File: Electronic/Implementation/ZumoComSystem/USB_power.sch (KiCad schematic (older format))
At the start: 9 parts, among them J2 USB_B_Micro, U6 R1218N021A

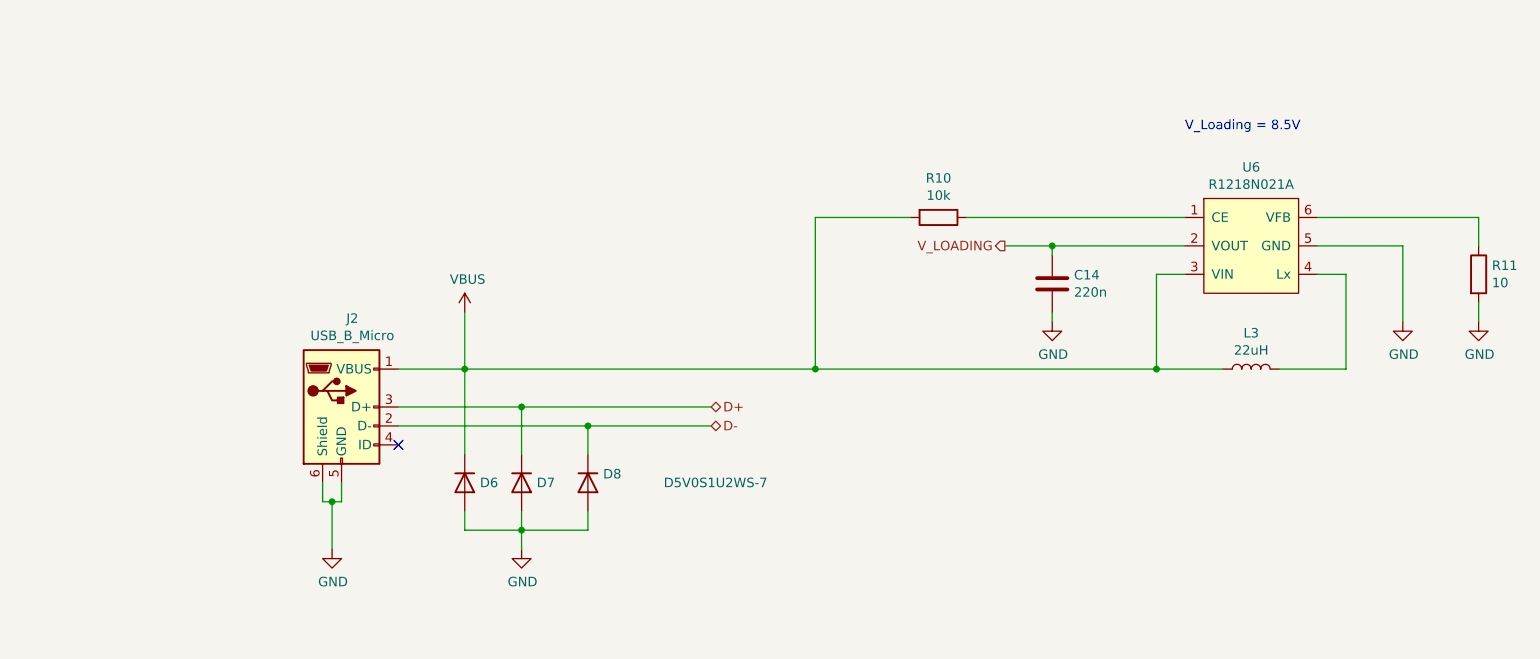
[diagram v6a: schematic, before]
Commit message: Electronic: implementation of the connector for external charging (reverse polarity protected)
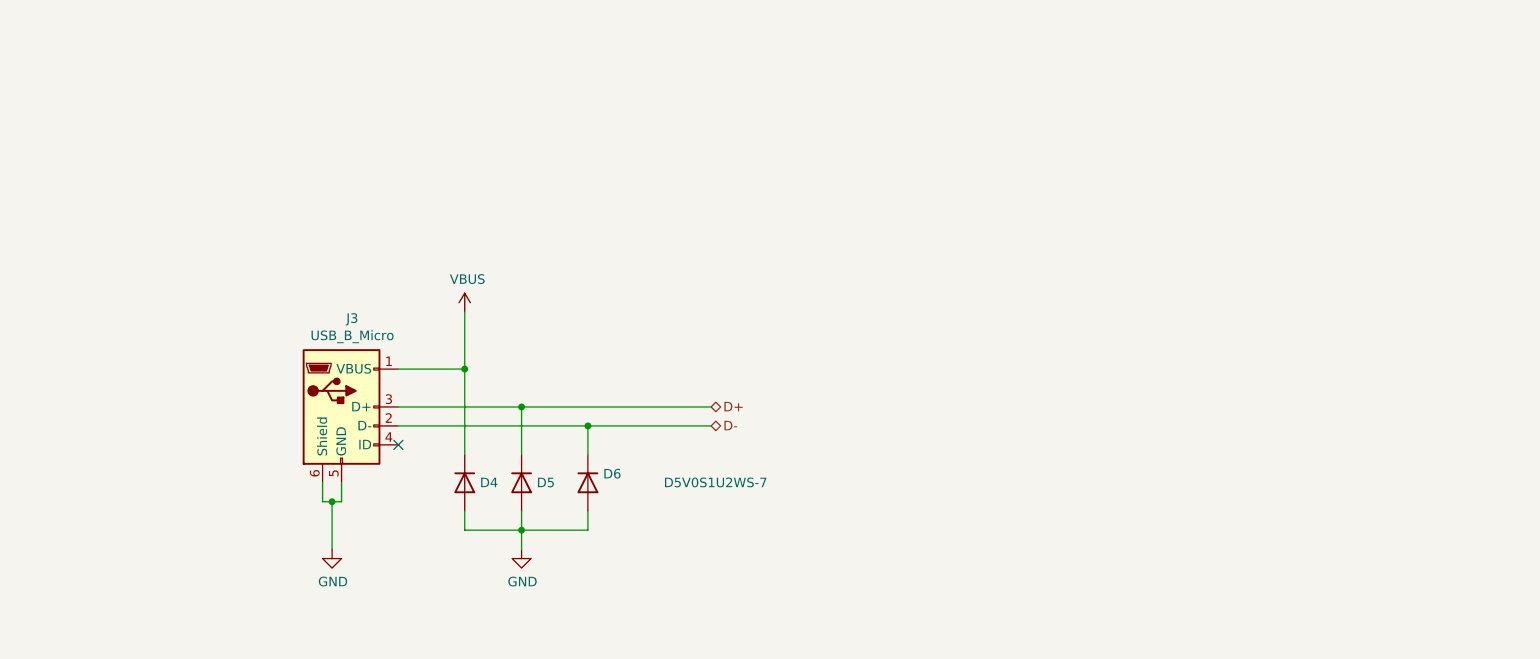
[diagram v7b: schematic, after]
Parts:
- removed C14: 220n, Capacitor_SMD:C_0603_1608Metric_Pad1.05x0.95mm_HandSolder, symbol Device:C
- removed L3: 22uH, footprints:L_Wuerth_HCI-1350_3D, symbol Device:L
- removed R10: 10k, Resistor_SMD:R_0603_1608Metric_Pad1.05x0.95mm_HandSolder, symbol Device:R
- removed R11: 10, Resistor_SMD:R_0603_1608Metric_Pad1.05x0.95mm_HandSolder, symbol Device:R
- removed U6: R1218N021A, Package_TO_SOT_SMD:SOT-23-6_Handsoldering, symbol LT1374CS8-5PBF:R1218N021A
- renumbered D6 to D4, D7 to D5, D8 to D6, J2 to J3
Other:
- note removed: "V_Loading = 8.5V"
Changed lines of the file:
@@
 Sheet 5 7
 Title "Zumo Communication System"
-Date "2022-03-08"
+Date "2022-03-25"
 Rev "V1.0"
 Comp "NewTec GmbH"
@@
 Comment4 ""
 $EndDescr
-Text HLabel 6000 2350 0    50   Output ~ 0
-V_LOADING
 Text HLabel 4450 3300 2    50   BiDi ~ 0
 D-
@@
 	2800 3200 3450 3200
 $Comp
-L Connector:USB_B_Micro J2
+L Connector:USB_B_Micro J3
 U 1 1 60DEC307
 P 2500 3200
-F 0 "J2" H 2557 3667 50  0000 C CNN
+F 0 "J3" H 2557 3667 50  0000 C CNN
 F 1 "USB_B_Micro" H 2557 3576 50  0000 C CNN
 F 2 "footprints:USB_Micro-B_Molex-105133-0001-3D" H 2650 3150 50  0001 C CNN
@@
 	2450 3700 2450 3950
 $Comp
-L power:GND #PWR030
+L power:GND #PWR026
 U 1 1 60DEDA4E
 P 2450 3950
-F 0 "#PWR030" H 2450 3700 50  0001 C CNN
+F 0 "#PWR026" H 2450 3700 50  0001 C CNN
 F 1 "GND" H 2455 3777 50  0000 C CNN
 F 2 "" H 2450 3950 50  0001 C CNN
@@
 NoConn ~ 2800 3400
 $Comp
-L LT1374CS8-5PBF:R1218N021A U6
-U 1 1 621F5235
-P 7300 2350
-F 0 "U6" H 7300 2765 50  0000 C CNN
-F 1 "R1218N021A" H 7300 2674 50  0000 C CNN
-F 2 "Package_TO_SOT_SMD:SOT-23-6_Handsoldering" H 7700 2700 50  0001 C CNN
-F 3 "https://www.nisshinbo-microdevices.co.jp/en/pdf/datasheet/r1218-ea.pdf" H 7700 2700 50  0001 C CNN
-	1    7300 2350
-	1    0    0    -1
-$EndComp
-Wire Wire Line
-	7650 2350 8100 2350
-Wire Wire Line
-	8100 2350 8100 2750
-$Comp
-L power:GND #PWR034
-U 1 1 621F66D3
-P 8100 2750
-F 0 "#PWR034" H 8100 2500 50  0001 C CNN
-F 1 "GND" H 8105 2577 50  0000 C CNN
-F 2 "" H 8100 2750 50  0001 C CNN
-F 3 "" H 8100 2750 50  0001 C CNN
-	1    8100 2750
-	1    0    0    -1
-$EndComp
-Wire Wire Line
-	6950 2350 6250 2350
-Wire Wire Line
-	6950 2200 5800 2200
-Wire Wire Line
-	5000 3000 6800 3000
-$Comp
-L Device:R R10
-U 1 1 621FAFF2
-P 5650 2200
-F 0 "R10" V 5443 2200 50  0000 C CNN
-F 1 "10k" V 5534 2200 50  0000 C CNN
-F 2 "Resistor_SMD:R_0603_1608Metric_Pad1.05x0.95mm_HandSolder" V 5580 2200 50  0001 C CNN
-F 3 "~" H 5650 2200 50  0001 C CNN
-	1    5650 2200
-	0    1    1    0
-$EndComp
-Wire Wire Line
-	5500 2200 5000 2200
-$Comp
-L Device:R R11
-U 1 1 621FB991
-P 8500 2500
-F 0 "R11" H 8570 2546 50  0000 L CNN
-F 1 "10" H 8570 2455 50  0000 L CNN
-F 2 "Resistor_SMD:R_0603_1608Metric_Pad1.05x0.95mm_HandSolder" V 8430 2500 50  0001 C CNN
-F 3 "~" H 8500 2500 50  0001 C CNN
-	1    8500 2500
-	1    0    0    -1
-$EndComp
-Wire Wire Line
-	7650 2200 8500 2200
-Wire Wire Line
-	6800 2500 6800 3000
-Wire Wire Line
-	6800 3000 7150 3000
-Wire Wire Line
-	6800 2500 6950 2500
-Wire Wire Line
-	7450 3000 7800 3000
-Wire Wire Line
-	7800 3000 7800 2500
-Wire Wire Line
-	7800 2500 7650 2500
-Wire Wire Line
-	8500 2650 8500 2750
-$Comp
-L power:GND #PWR035
-U 1 1 621FE4AA
-P 8500 2750
-F 0 "#PWR035" H 8500 2500 50  0001 C CNN
-F 1 "GND" H 8505 2577 50  0000 C CNN
-F 2 "" H 8500 2750 50  0001 C CNN
-F 3 "" H 8500 2750 50  0001 C CNN
-	1    8500 2750
-	1    0    0    -1
-$EndComp
-Wire Wire Line
-	8500 2200 8500 2350
-Connection ~ 5000 3000
-Connection ~ 6800 3000
-Wire Wire Line
-	5000 2200 5000 3000
-$Comp
-L Device:C C14
-U 1 1 62201332
-P 6250 2550
-F 0 "C14" H 6365 2596 50  0000 L CNN
-F 1 "220n" H 6365 2505 50  0000 L CNN
-F 2 "Capacitor_SMD:C_0603_1608Metric_Pad1.05x0.95mm_HandSolder" H 6288 2400 50  0001 C CNN
-F 3 "~" H 6250 2550 50  0001 C CNN
-	1    6250 2550
-	1    0    0    -1
-$EndComp
-Wire Wire Line
-	6250 2700 6250 2750
-Wire Wire Line
-	6250 2400 6250 2350
-Connection ~ 6250 2350
-Wire Wire Line
-	6250 2350 6000 2350
-$Comp
-L power:GND #PWR033
-U 1 1 62201F1D
-P 6250 2750
-F 0 "#PWR033" H 6250 2500 50  0001 C CNN
-F 1 "GND" H 6255 2577 50  0000 C CNN
-F 2 "" H 6250 2750 50  0001 C CNN
-F 3 "" H 6250 2750 50  0001 C CNN
-	1    6250 2750
-	1    0    0    -1
-$EndComp
-Text Notes 6950 1750 0    50   ~ 0
-V_Loading = 8.5V
-$Comp
-L power:VBUS #PWR031
+L power:VBUS #PWR027
 U 1 1 6230EF27
 P 3150 2700
-F 0 "#PWR031" H 3150 2550 50  0001 C CNN
+F 0 "#PWR027" H 3150 2550 50  0001 C CNN
 F 1 "VBUS" H 3165 2873 50  0000 C CNN
 F 2 "" H 3150 2700 50  0001 C CNN
@@
 	2800 3000 3150 3000
 Connection ~ 3150 3000
-Wire Wire Line
-	3150 3000 5000 3000
 $Comp
-L Device:D D7
+L Device:D D5
 U 1 1 6235853C
 P 3450 3600
-F 0 "D7" V 3450 3680 50  0000 L CNN
+F 0 "D5" V 3450 3680 50  0000 L CNN
 F 1 "D5V0S1U2WS-7" V 3495 3680 50  0001 L CNN
 F 2 "Diode_SMD:D_SOD-323_HandSoldering" H 3450 3600 50  0001 C CNN
@@
 $EndComp
 $Comp
-L Device:D D8
+L Device:D D6
 U 1 1 62358EEE
 P 3800 3600
-F 0 "D8" V 3754 3680 50  0000 L CNN
+F 0 "D6" V 3754 3680 50  0000 L CNN
 F 1 "D5V0S1U2WS-7" V 3800 4000 50  0000 L CNN
 F 2 "Diode_SMD:D_SOD-323_HandSoldering" H 3800 3600 50  0001 C CNN
@@
 	3800 3300 4450 3300
 $Comp
-L Device:D D6
+L Device:D D4
 U 1 1 62359ADA
 P 3150 3600
-F 0 "D6" V 3150 3680 50  0000 L CNN
+F 0 "D4" V 3150 3680 50  0000 L CNN
 F 1 "D5V0S1U2WS-7" V 3195 3680 50  0001 L CNN
 F 2 "Diode_SMD:D_SOD-323_HandSoldering" H 3150 3600 50  0001 C CNN
@@
 	3150 3450 3150 3000
 $Comp
-L power:GND #PWR032
+L power:GND #PWR028
 U 1 1 6235AC4B
 P 3450 3950
-F 0 "#PWR032" H 3450 3700 50  0001 C CNN
+F 0 "#PWR028" H 3450 3700 50  0001 C CNN
 F 1 "GND" H 3455 3777 50  0000 C CNN
 F 2 "" H 3450 3950 50  0001 C CNN
@@
 Wire Wire Line
 	3450 3850 3450 3950
-$Comp
-L Device:L L?
-U 1 1 623D0E3C
-P 7300 3000
-AR Path="/60C4F1BF/623D0E3C" Ref="L?"  Part="1"
-AR Path="/60C3F428/623D0E3C" Ref="L3"  Part="1"
-F 0 "L3" V 7490 3000 50  0000 C CNN
-F 1 "22uH" V 7399 3000 50  0000 C CNN
-F 2 "footprints:L_Wuerth_HCI-1350_3D" H 7300 3000 50  0001 C CNN
-F 3 "https://www.vishay.com/docs/34282/ihlp-6767gz-11.pdf" H 7300 3000 50  0001 C CNN
-	1    7300 3000
-	0    -1   -1   0
-$EndComp
 $EndSCHEMATC

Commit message: Coutouts, BOM, ...
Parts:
- D4, D5, D6: Manufacturer (none) -> Diodes Incorporated; Part-No. (none) -> D5V0S1U2WS-7
- J3: Manufacturer (none) -> Molex; Part-No. (none) -> 1051330001
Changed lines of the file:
@@
 Sheet 5 7
 Title "Zumo Communication System"
-Date "2022-03-25"
+Date "2022-04-15"
 Rev "V1.0"
 Comp "NewTec GmbH"
@@
 F 2 "footprints:USB_Micro-B_Molex-105133-0001-3D" H 2650 3150 50  0001 C CNN
 F 3 "~" H 2650 3150 50  0001 C CNN
+F 4 "Molex" H 2500 3200 50  0001 C CNN "Manufacturer"
+F 5 "1051330001" H 2500 3200 50  0001 C CNN "Part-No."
 	1    2500 3200
 	1    0    0    -1
@@
 F 2 "Diode_SMD:D_SOD-323_HandSoldering" H 3450 3600 50  0001 C CNN
 F 3 "https://www.diodes.com/assets/Datasheets/D5V0S1U2WS.pdf" H 3450 3600 50  0001 C CNN
+F 4 "Diodes Incorporated" H 3450 3600 50  0001 C CNN "Manufacturer"
+F 5 "D5V0S1U2WS-7" H 3450 3600 50  0001 C CNN "Part-No."
 	1    3450 3600
 	0    1    1    0
@@
 F 2 "Diode_SMD:D_SOD-323_HandSoldering" H 3800 3600 50  0001 C CNN
 F 3 "https://www.diodes.com/assets/Datasheets/D5V0S1U2WS.pdf" H 3800 3600 50  0001 C CNN
+F 4 "Diodes Incorporated" H 3800 3600 50  0001 C CNN "Manufacturer"
+F 5 "D5V0S1U2WS-7" H 3800 3600 50  0001 C CNN "Part-No."
 	1    3800 3600
 	0    1    1    0
@@
 F 2 "Diode_SMD:D_SOD-323_HandSoldering" H 3150 3600 50  0001 C CNN
 F 3 "https://www.diodes.com/assets/Datasheets/D5V0S1U2WS.pdf" H 3150 3600 50  0001 C CNN
+F 4 "Diodes Incorporated" H 3150 3600 50  0001 C CNN "Manufacturer"
+F 5 "D5V0S1U2WS-7" H 3150 3600 50  0001 C CNN "Part-No."
 	1    3150 3600
 	0    1    1    0
